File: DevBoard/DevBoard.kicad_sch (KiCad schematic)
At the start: 49 parts, among them J1 12V, J2 USB C, U1 STM32F103T6Ux, U2 TPS54202DDC, U3 TLV75533PDBV

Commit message: Initial layout/schematic
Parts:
- removed U1: STM32F103T6Ux, Package_DFN_QFN:QFN-36-1EP_6x6mm_P0.5mm_EP4.1x4.1mm, symbol MCU_ST_STM32F1:STM32F103T6Ux
- added C13, C14: 10p, Capacitor_SMD:C_0603_1608Metric_Pad1.08x0.95mm_HandSolder, symbol Device:C_Small
- added C15, C16, C17, C18, C19, C20: 0.1u, Capacitor_SMD:C_0603_1608Metric_Pad1.08x0.95mm_HandSolder, symbol Device:C_Small
- added C21: 4.7u, Capacitor_SMD:C_0805_2012Metric_Pad1.18x1.45mm_HandSolder, symbol Device:C_Small
- added J3: JTAG/SWD, Connector_PinHeader_1.27mm:PinHeader_2x07_P1.27mm_Vertical_SMD, symbol Connector_Generic:Conn_02x07_Odd_Even
- added J4: Conn_01x12, Connector_PinHeader_2.54mm:PinHeader_1x12_P2.54mm_Vertical, symbol Connector_Generic:Conn_01x12
- added R10: 1k, Resistor_SMD:R_0402_1005Metric_Pad0.72x0.64mm_HandSolder, symbol Device:R_Small
- added R11, R12, R13, R14, R16: 10k, Resistor_SMD:R_0603_1608Metric_Pad0.98x0.95mm_HandSolder, symbol Device:R_Small
- added R15: 100k, Resistor_SMD:R_0603_1608Metric_Pad0.98x0.95mm_HandSolder, symbol Device:R_Small
- added R17: 100, Resistor_SMD:R_0603_1608Metric_Pad0.98x0.95mm_HandSolder, symbol Device:R_Small
- added SW1, SW2: SW_SPDT, symbol Switch:SW_SPDT
- added SW3: SW_Push, symbol Switch:SW_Push
- added TP10, TP11, TP12, TP13, TP16, TP8, TP9: TestPoint, TestPoint:TestPoint_Pad_D2.0mm, symbol Connector:TestPoint
- added U1: STM32F103C6Tx, Package_QFP:LQFP-48_7x7mm_P0.5mm, symbol MCU_ST_STM32F1:STM32F103C6Tx
- added Y1: 8MHz, Crystal:Crystal_SMD_Abracon_ABM8G-4Pin_3.2x2.5mm, symbol Device:Crystal_GND24
- U4: footprint (none) -> CustomKicadFootprints:SAM-M10Q
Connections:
- net +12V_D: now also J4.1 (Pin_1), R15.1
- net +3V3: now also C16.1, C17.1, C18.1, C19.1, C20.1, C21.1, J3.3 (Pin_3), J4.3 (Pin_3), R13.1, R14.2, SW1.3 (C), SW2.3 (C), U1.1 (VBAT), U1.24 (VDD), U1.36 (VDD), U1.48 (VDD), U1.9 (VDDA)
- net +5V: now also J4.2 (Pin_2)
- net GND: now also C13.1, C14.1, C15.2, C16.2, C17.2, C18.2, C19.2, C20.2, C21.2, J3.2 (Pin_2), J3.5 (Pin_5), J3.7 (Pin_7), J4.4 (Pin_4), R16.2, R17.1, SW1.1 (A), SW2.1 (A), SW3.1, U1.23 (VSS), U1.35 (VSS), U1.47 (VSS), U1.8 (VSSA), Y1.1, Y1.3
- net GPS_INT: now also U1.10 (PA0)
- net GPS_RST: now also R14.1, TP13.1, U1.45 (PB8)
- net GPS_RX: now also TP12.1, U1.31 (PA10)
- net GPS_SAFEBOOT: now also U4.8 (SAFEBOOT), TP16.1, U1.41 (PB5); no longer U4.7 (SAFEBOOT)
- net GPS_TIMEPULSE: now also U1.46 (PB9)
- net GPS_TX: now also TP11.1, U1.30 (PA9)
- net SCL: now also U1.42 (PB6)
- net SDA: now also U1.43 (PB7)
- net USB_DN: now also U1.32 (PA11)
- net USB_DP: now also U1.33 (PA12)
- new net: C13.2, U1.5 (PD0), Y1.2
- new net: C14.2, R10.1, Y1.4
- new net: R12.1, SW2.2 (B), TP8.1
- new net: J3.11 (Pin_11), R17.2
- new net: R11.1, SW1.2 (B), TP9.1
- new net: R10.2, U1.6 (PD1)
- new net BOOT0: R11.2, U1.44 (BOOT0)
- new net BOOT1: R12.2, U1.20 (PB2)
- new net JTAG_NRST: J3.12 (Pin_12), U1.40 (PB4)
- new net JTAG_TCK: J3.6 (Pin_6), U1.37 (PA14)
- new net JTAG_TDI: J3.10 (Pin_10), U1.38 (PA15)
- new net JTAG_TDO: J3.8 (Pin_8), U1.39 (PB3)
- new net JTAG_TMS: J3.4 (Pin_4), U1.34 (PA13)
- new net NRST: C15.1, R13.2, SW3.2, TP10.1, U1.7 (NRST)
- new net PA1: J4.9 (Pin_9), U1.11 (PA1)
- new net PA2: J4.8 (Pin_8), U1.12 (PA2)
- new net PA5: J4.7 (Pin_7), U1.15 (PA5)
- new net PA6: J4.6 (Pin_6), U1.16 (PA6)
- new net PA7: J4.5 (Pin_5), U1.17 (PA7)
- new net PC13: J4.12 (Pin_12), U1.2 (PC13)
- new net PC14: J4.11 (Pin_11), U1.3 (PC14)
- new net PC15: J4.10 (Pin_10), U1.4 (PC15)
- new net aIN_12V_READ: R15.2, R16.1
- no-connect marks 2 -> 15
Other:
- company: (none) -> MD
- title: (none) -> DevBoard
- moved on the sheet: C1, C2, C3, C4, C5, C6, C7, C8, D1, D3, D4, D5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

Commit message: Updates to DRC/schematic/layout. Layout to be redone.
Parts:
- removed C10, C11, C12: 0.1u, Capacitor_SMD:C_0603_1608Metric_Pad1.08x0.95mm_HandSolder, symbol Device:C_Small
- removed C9: 10U, Capacitor_SMD:C_0805_2012Metric_Pad1.18x1.45mm_HandSolder, symbol Device:C_Small
- removed J1: 12V, Connector_BarrelJack:BarrelJack_Wuerth_6941xx301002, symbol Connector:Barrel_Jack
- removed J2: USB C, Connector_USB:USB_C_Receptacle_GCT_USB4110, symbol Connector:USB_C_Receptacle_USB2.0_16P
- removed SW1, SW2: SW_SPDT, symbol Switch:SW_SPDT
- removed SW3: SW_Push, symbol Switch:SW_Push
- removed U1: STM32F103C6Tx, Package_QFP:LQFP-48_7x7mm_P0.5mm, symbol MCU_ST_STM32F1:STM32F103C6Tx
- added D10: BLUE, LED_SMD:LED_0603_1608Metric_Pad1.05x0.95mm_HandSolder, symbol Device:LED_Small_Filled
- added J1: UJ20-C-H-G-SMT-2A-P16-TR, CustomKicadFootprints:UJ20-C-H-G-SMT-2A-P16-TR, symbol PartDB:UJ20-C-H-G-SMT-2A-P16-TR
- added J5: PRT-00119, CustomKicadFootprints:BarrelJack_3Pin_PJ202A, symbol PartDB:PRT-00119
- added R18: 1k, Resistor_SMD:R_0603_1608Metric_Pad0.98x0.95mm_HandSolder, symbol Device:R_Small
- added R19, R20: 4.7k, Resistor_SMD:R_0603_1608Metric_Pad0.98x0.95mm_HandSolder, symbol Device:R_Small
- added SW2, SW4: SLW-88229-2-SMT-TR, CustomKicadFootprints:SLW-88229-2-SMT-TR, symbol PartDB:SLW-88229-2-SMT-TR
- added U1: STM32F103C6T7A, Package_QFP:LQFP-48_7x7mm_P0.5mm, symbol PartDB:STM32F103C6T7A
- added U5: TE 1571563-6, CustomKicadFootprints:506-1571563-6, symbol PartDB:TE 1571563-6
- D1, D5, D6, D9: footprint (none) -> LED_SMD:LED_0603_1608Metric_Pad1.05x0.95mm_HandSolder
- TP1, TP10, TP11, TP12, TP13, TP16, TP2, TP3, TP4, TP5, TP6, TP7, TP8, TP9: footprint TestPoint:TestPoint_Pad_D2.0mm -> TestPoint:TestPoint_Pad_D1.0mm
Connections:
- net +12V: now also J5.1
- net +3V3: now also R18.1, R19.1, R20.1, SW2.3 (C), SW4.3 (C), U1.1 (VBAT), U1.24 (VDD), U1.36 (VDD), U1.48 (VDD), U1.9 (VDDA)
- net BOOT0: now also U1.44 (BOOT0)
- net BOOT1: now also U1.20 (PB2)
- net GND: now also D10.1 (K), J1.A1 (GND), J1.A12 (GND), J1.B1 (GND), J1.B12 (GND), J1.S1 (SHIELD), J5.2, SW2.1 (A), SW4.1 (A), U1.23 (VSS), U1.35 (VSS), U1.47 (VSS), U1.8 (VSSA), U5.1
- net GPS_INT: now also U1.10 (PA0)
- net GPS_RST: now also U1.45 (PB8)
- net GPS_RX: now also U1.31 (PA10)
- net GPS_SAFEBOOT: now also U1.41 (PB5)
- net GPS_TIMEPULSE: now also U1.46 (PB9)
- net GPS_TX: now also U1.30 (PA9)
- net JTAG_NRST: now also U1.40 (PB4)
- net JTAG_TCK: now also U1.37 (PA14)
- net JTAG_TDI: now also U1.38 (PA15)
- net JTAG_TDO: now also U1.39 (PB3)
- net JTAG_TMS: now also U1.34 (PA13)
- net NRST: now also U1.7 (NRST), U5.2
- net PA1: now also U1.11 (PA1)
- net PA2: now also U1.12 (PA2)
- net PA5: now also U1.15 (PA5)
- net PA6: now also U1.16 (PA6)
- net PA7: now also U1.17 (PA7)
- net PC13: now also U1.2 (PC13)
- net PC14: now also U1.3 (PC14)
- net PC15: now also U1.4 (PC15)
- net SCL: now also R20.2, U1.42 (PB6)
- net SDA: now also R19.2, U1.43 (PB7)
- net USB_DN: now also J1.A7 (D-), J1.B7 (D-), U1.32 (PA11)
- net USB_DP: now also J1.A6 (D+), J1.B6 (D+), U1.33 (PA12)
- net aIN_12V_READ: now also U1.13 (PA3)
- net at C13.2, Y1.2: now also U1.5 (PD0)
- net at R12.1, TP8.1: now also SW2.2 (B)
- net at R11.1, TP9.1: now also SW4.2 (B)
- net at R2.1: now also J1.A5 (CC1)
- net at F1.1: now also J1.A4 (VBUS), J1.A9 (VBUS), J1.B4 (VBUS), J1.B9 (VBUS)
- net at R3.1: now also J1.B5 (CC2)
- net at R10.2: now also U1.6 (PD1)
- new net: D10.2 (A), R18.2
- no-connect marks 15 -> 14
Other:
- moved on the sheet: C7, C8, D9, R9, TP11, TP5, TP6, U3, U4

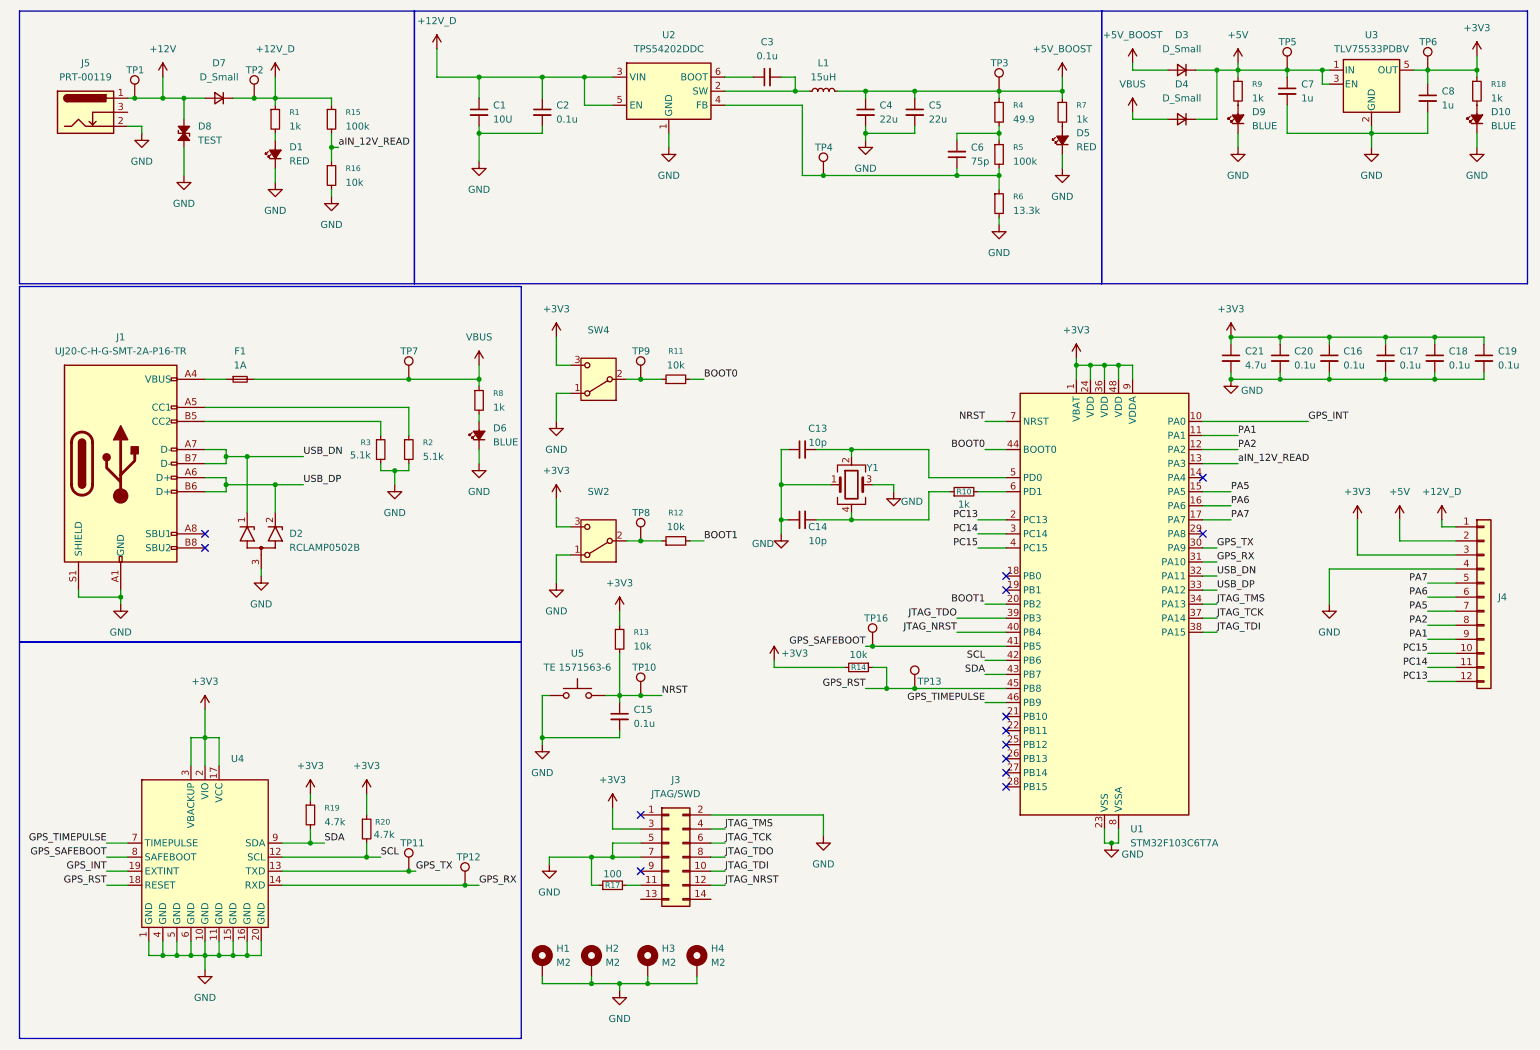
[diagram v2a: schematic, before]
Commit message: A0.1 layout (not happy, will be redone again)
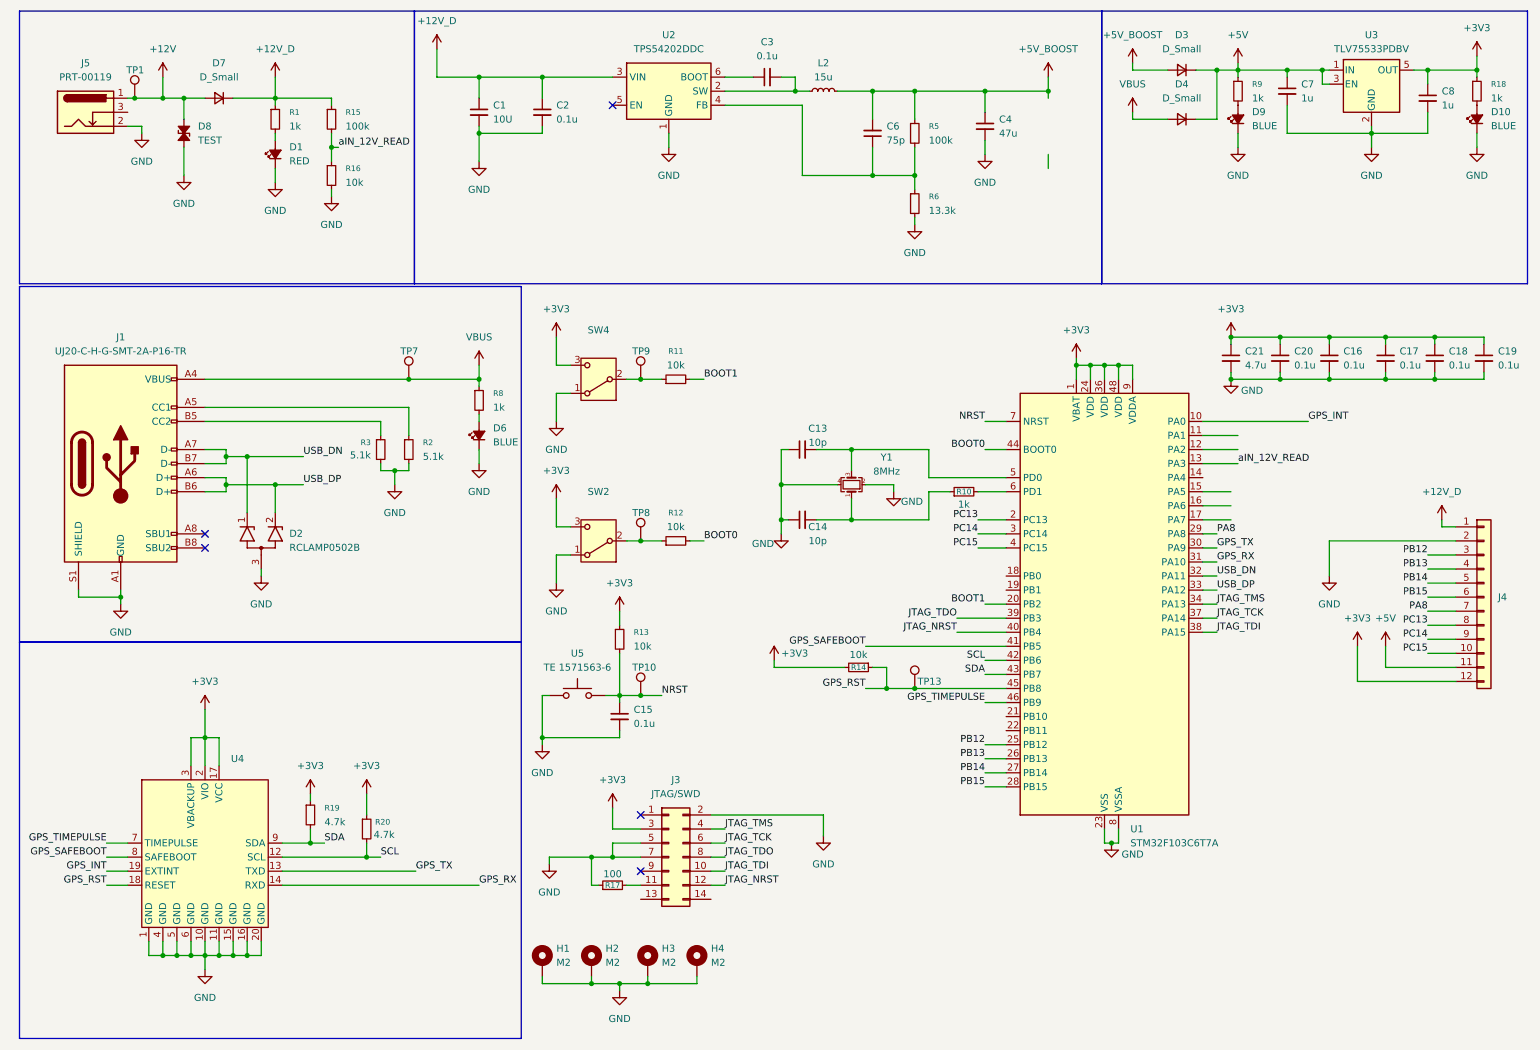
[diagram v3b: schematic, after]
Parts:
- removed C5: 22u, Capacitor_SMD:C_0805_2012Metric_Pad1.18x1.45mm_HandSolder, symbol Device:C_Small
- removed D5: RED, LED_SMD:LED_0603_1608Metric_Pad1.05x0.95mm_HandSolder, symbol Device:LED_Small_Filled
- removed F1: 1A, Fuse:Fuse_0805_2012Metric_Pad1.15x1.40mm_HandSolder, symbol Device:Fuse_Small
- removed L1: 15uH, Inductor_SMD:L_Coilcraft_LPS3314, symbol Device:L_Small
- removed R4: 49.9, Resistor_SMD:R_0603_1608Metric_Pad0.98x0.95mm_HandSolder, symbol Device:R_Small
- removed R7: 1k, Resistor_SMD:R_0603_1608Metric_Pad0.98x0.95mm_HandSolder, symbol Device:R_Small
- removed TP11, TP12, TP16, TP2, TP3, TP4, TP5, TP6: TestPoint, TestPoint:TestPoint_Pad_D1.0mm, symbol Connector:TestPoint
- removed Y1: 8MHz, Crystal:Crystal_SMD_Abracon_ABM8G-4Pin_3.2x2.5mm, symbol Device:Crystal_GND24
- added L2: 15u, CustomKicadFootprints:L_Coilcraft_XAL40, symbol PartDB:XAL4040-153MEC
- added Y1: 8MHz, CustomKicadFootprints:Crystal_FC3BA, symbol PartDB:FC3BAEBDI8.0-T1
- C4: value 22u -> 47u
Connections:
- net +12V_D: no longer U2.5 (EN)
- net +3V3: now also J4.12 (Pin_12); no longer J4.3 (Pin_3)
- net +5V: now also J4.11 (Pin_11); no longer J4.2 (Pin_2)
- net +5V_BOOST: now also C6.2, R5.1, L2.2
- net BOOT0: now also R12.2; no longer R11.2
- net BOOT1: now also R11.2; no longer R12.2
- net GND: now also J4.2 (Pin_2), Y1.2, Y1.4; no longer J4.4 (Pin_4)
- net PC13: now also J4.8 (Pin_8); no longer J4.12 (Pin_12)
- net PC14: now also J4.9 (Pin_9); no longer J4.11 (Pin_11)
- net VBUS: now also J1.A4 (VBUS), J1.A9 (VBUS), J1.B4 (VBUS), J1.B9 (VBUS)
- net at C13.2, U1.5 (PD0): now also Y1.3
- net at C14.2, R10.1: now also Y1.1
- net at C3.2, U2.2 (SW): now also L2.1
- net PB12: now reaches U1.25 (PB12)
- net PB12: now also J4.3 (Pin_3)
- net PB13: now reaches U1.26 (PB13)
- net PB13: now also J4.4 (Pin_4)
- net PB14: now reaches U1.27 (PB14)
- net PB14: now also J4.5 (Pin_5)
- net PB15: now reaches U1.28 (PB15)
- net PB15: now also J4.6 (Pin_6)
- net PA8: now reaches U1.29 (PA8)
- net PA8: now also J4.7 (Pin_7)
- net PA1: no longer names the net of U1.11 (PA1)
- net PA1: no longer J4.9 (Pin_9)
- net PA2: no longer names the net of U1.12 (PA2)
- net PA2: no longer J4.8 (Pin_8)
- net PA5: no longer names the net of U1.15 (PA5)
- net PA5: no longer J4.7 (Pin_7)
- net PA6: no longer names the net of U1.16 (PA6)
- net PA6: no longer J4.6 (Pin_6)
- net PA7: no longer names the net of U1.17 (PA7)
- net PA7: no longer J4.5 (Pin_5)
- no-connect marks 14 -> 5
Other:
- moved on the sheet: C4, C6, R5, R6
